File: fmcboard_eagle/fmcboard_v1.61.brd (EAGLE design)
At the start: 147 x 74 mm, 202 parts, among them IC1 OPA695IDR, IC10 LM358, IC11 7805TV, IC12 SN74AUC2G66DCTR, IC13 SN74AUC2G66DCTR, IC14 SN74AUC2G66DCTR, IC15 SN74AUC2G66DCTR, IC16 DAC7578SPWR, IC17 SN74AUC2G66DCTR, IC18 SN74AUC2G66DCTR, IC19 SN74AUC2G66DCTR, IC2 DAC7578SPWR, IC20 SN74AUC2G66DCTR, IC21 74AUP2GU04GW, IC22 74AUP2GU04GW, IC23 74AUP2GU04GW, IC24 74AUP2GU04GW, IC26 AMS1117-1.8, IC27 OPA699ID, IC3 LTC6229IMS8E#TRPBF, IC4 OPA695IDR, IC5 LTC6229IMS8E#TRPBF, IC6 OPA695IDR, IC7 OPA699ID, IC8 LM358, IC9 LM358, J1 8pin, J12 4p-2.54, J2 ASP-134604-01, J3 4p-2.54, J4 4p-2.54, J5 8pin, J6 4p-2.54, J7 4p-2.54, J8 4p-2.54, J9 8pin, U1 TXS0108EPWR, U2 STMICROELECTRONICS_L7905ACVST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

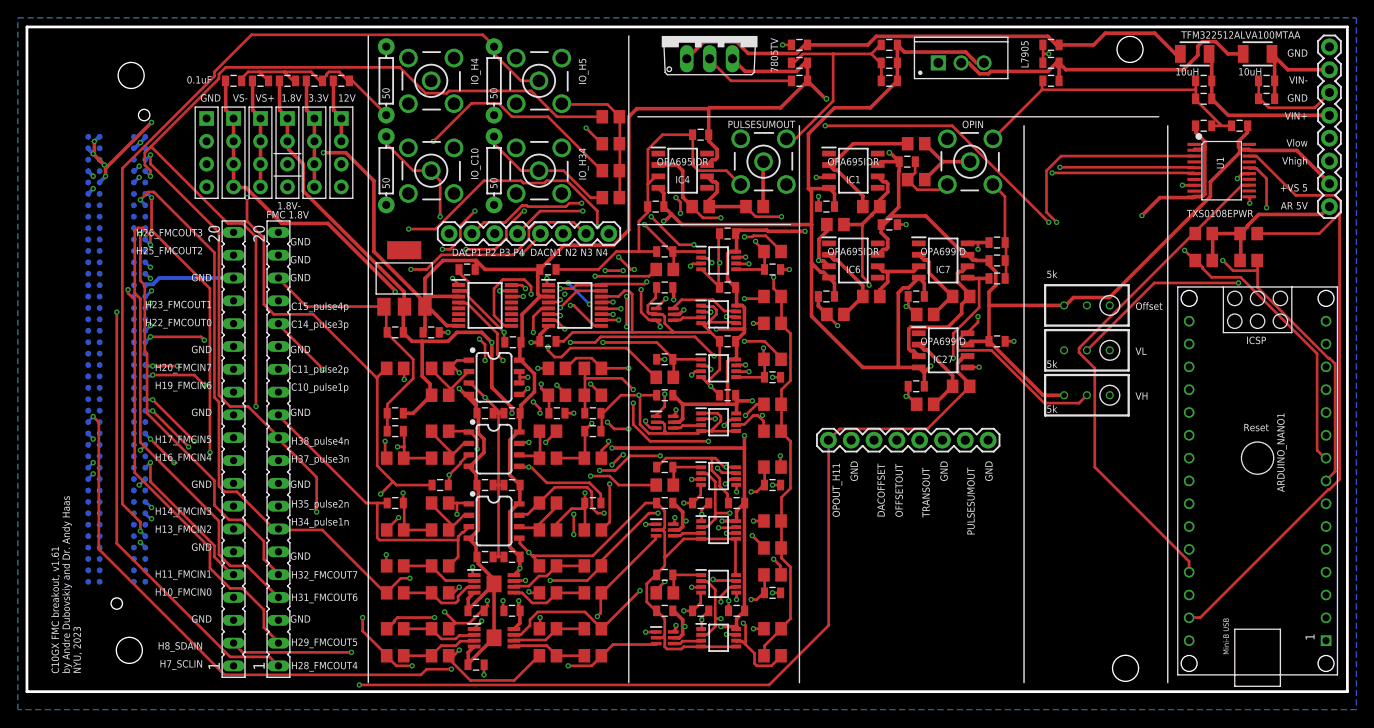
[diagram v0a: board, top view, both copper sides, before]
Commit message: use 1.8- and gnd for negative switches to gnd add 100 ohm resistors to inverting opa695s
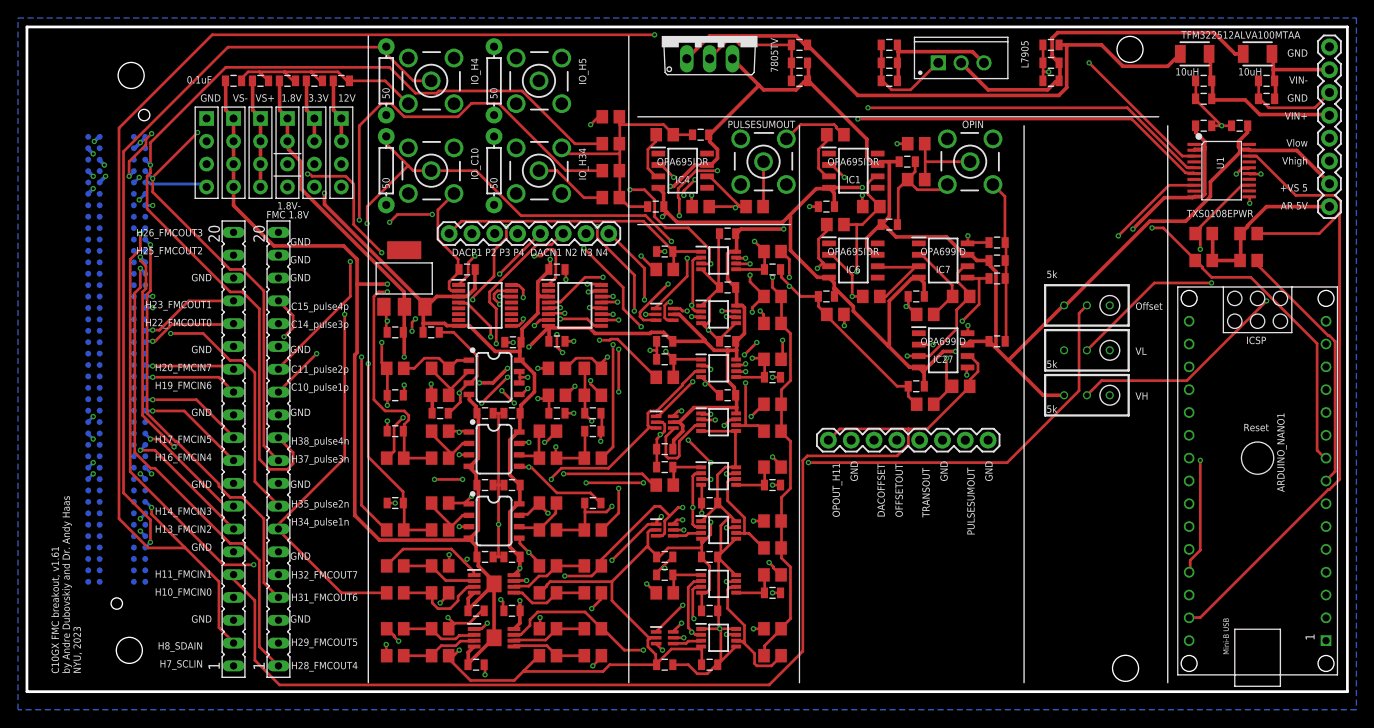
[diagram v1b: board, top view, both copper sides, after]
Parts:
- added R13, R3: 100, rcl:R0805
- moved C70 48.5 mm to (71.0, 3.00), turned to 0 degrees
- moved C35 42.6 mm to (78.0, 51.0)
- moved C77 31.0 mm to (76.0, 15.0)
- moved C36 26.9 mm to (46.0, 31.0), turned to 0 degrees
- moved C49 19.7 mm to (71.0, 27.0)
- moved C71 18.0 mm to (71.0, 15.0), turned to 0 degrees
- moved C51 12.0 mm to (76.0, 9.00)
- moved C34 9.00 mm to (41.0, 40.0)
- moved C66 7.00 mm to (41.0, 33.0), turned to 0 degrees
- moved C50 6.08 mm to (76.0, 3.00)
- moved C68 6.00 mm to (71.0, 39.0)
- moved C67 3.00 mm to (76.0, 21.0), turned to 0 degrees
- moved C14 1.00 mm to (59.0, 39.0)
- moved C54 1.00 mm to (59.0, 47.0)
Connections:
- removed net H10: J2.H10, SV1.4
- removed net OP2BUF: IC27.3, IC7.6, R6.2
- new net N$3: IC1.3, R3.1
- new net N$8: IC4.3, R13.1
- new net OPOUT_H10: IC27.3, IC7.6, J2.H10, R6.2, SV1.4
- net 1V8: no longer C66.1, C67.1, C70.1, C71.1, IC19.8, IC20.8, IC22.5, IC24.5
- net 1V8-: now also C66.1, C67.1, C70.1, C71.1, IC19.4, IC20.4, IC22.2, IC24.2
- net GND: now also IC19.8, IC20.8, IC22.5, IC24.5, R13.2, R3.2; no longer IC1.3, IC19.4, IC20.4, IC22.2, IC24.2, IC4.3
- net H34: no longer IC22.1
- net H34I: now also IC22.1
- net H35: no longer IC22.3
- net H35I: now also IC22.3
- net H37: no longer IC24.1
- net H37I: now also IC24.1
- net H38: no longer IC24.3
- net H38I: now also IC24.3
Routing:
- net OPOUT_H10: track 0.00 -> 147.1 mm, vias 0 -> 2
- net GND: track 524.9 -> 380.8 mm, vias 35 -> 42
- net C15: track 166.2 -> 92.0 mm, vias 4 -> 5
- net 1V8: track 260.9 -> 187.8 mm, vias 15 -> 7
- net SCLIN: track 209.8 -> 161.7 mm
- net H37: track 163.5 -> 120.3 mm, vias 5 -> 4
- net N$2: track 115.4 -> 74.3 mm, vias 7 -> 4
- net H34: track 154.4 -> 113.5 mm, vias 3 -> 2
- net SDAIN: track 174.6 -> 201.6 mm
- net VS+: track 301.5 -> 278.8 mm
- net VS-: track 259.7 -> 280.7 mm
- net C14: track 114.6 -> 94.3 mm, vias 8 -> 3
- net H10: track 17.8 -> 0.00 mm, vias 1 -> 0
- net AR_SDAIN2: track 150.7 -> 168.4 mm, vias 5 -> 4
- net OP2BUF: track 17.1 -> 0.00 mm
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
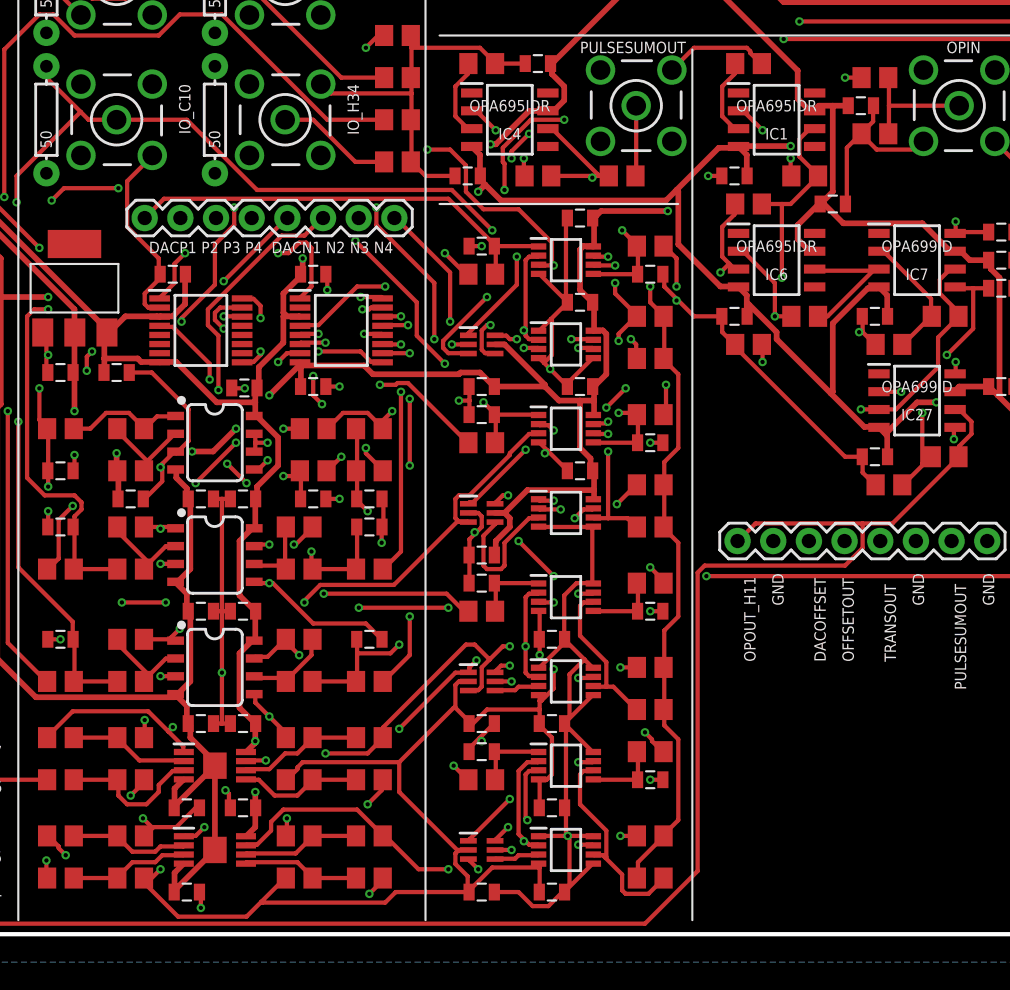
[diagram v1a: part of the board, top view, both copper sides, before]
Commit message: add dac pulse offsets + and -
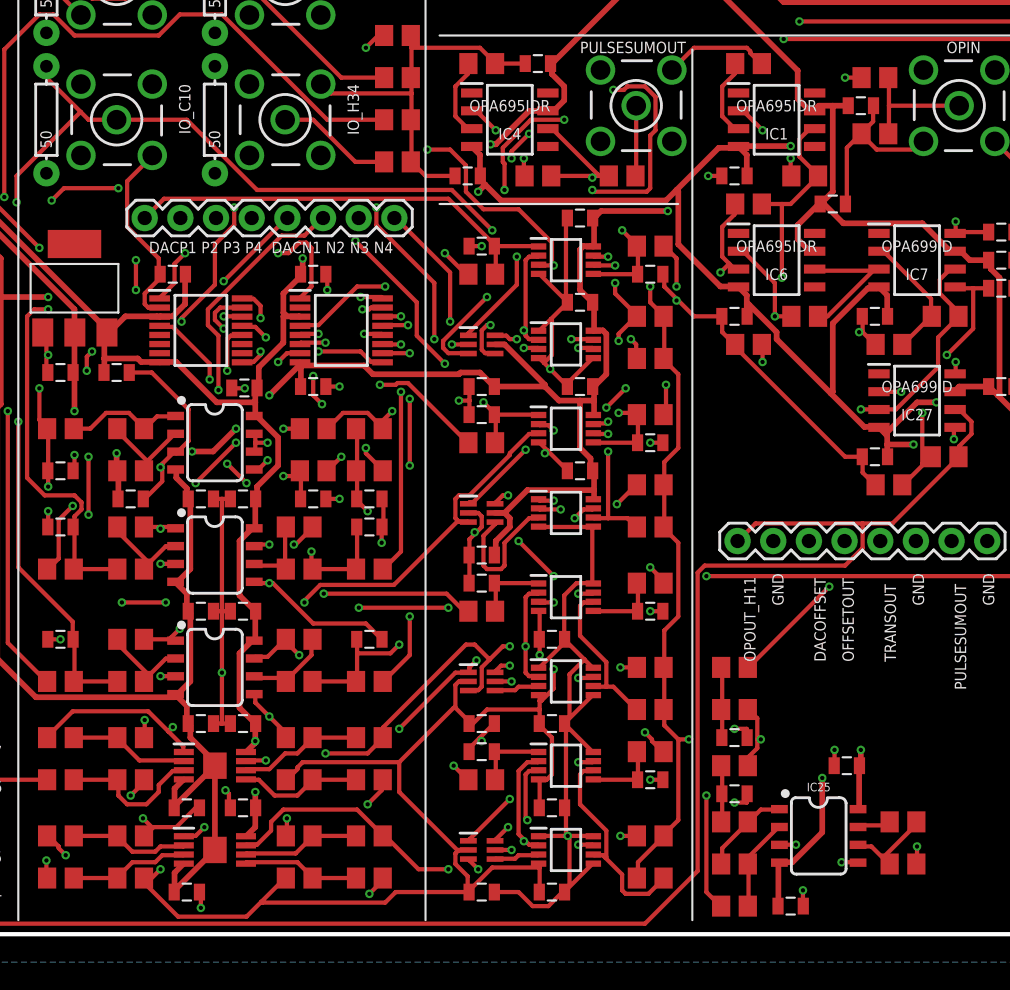
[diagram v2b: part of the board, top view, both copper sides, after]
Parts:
- added C11, C80: 1uF, SparkFun-Passives:0805
- added C33, C65: 0.1uF, SparkFun-Passives:0805
- added IC25: LM358, SparkFun-IC-Amplifiers:SO08
- added R14, R35, R61, R70, R79, R85: 1k, rcl:R0805
- added R73, R84: 100, rcl:R0805
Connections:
- new net N$30: IC25.7, R14.2
- new net N$36: IC25.1, R35.2, R73.2
- new net N$37: IC25.2, R35.1, R61.1
- new net N$38: IC25.6, R14.1, R70.1
- new net N$39: IC16.13, R84.2
- new net PULSEOFFSET_N: IC16.12, R61.2
- new net PULSEOFFSET_NI: C11.2, R73.1, R85.2
- new net PULSEOFFSET_P: C80.1, R79.2, R84.1
- net GND: now also C11.1, C33.2, C65.2, C80.2, IC25.3, IC25.5, R70.2
- net PULSESUMIN: now also R79.1, R85.1
- net VS+: now also C33.1, IC25.8
- net VS-: now also C65.1, IC25.4
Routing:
- net N$39: track 0.00 -> 121.9 mm, vias 0 -> 6
- net PULSEOFFSET_N: track 0.00 -> 94.0 mm, vias 0 -> 4
- net VS-: track 280.7 -> 325.2 mm, vias 4 -> 6
- net VS+: track 278.8 -> 310.3 mm, vias 5 -> 6
- net PULSESUMIN: track 65.5 -> 76.3 mm, vias 3 -> 5
- net GND: track 380.8 -> 389.8 mm, vias 42 -> 49
- net N$38: track 0.00 -> 6.99 mm
- net N$37: track 0.00 -> 6.69 mm
- net N$36: track 0.00 -> 6.44 mm
- net PULSEOFFSET_P: track 0.00 -> 5.20 mm
- net PULSEOFFSET_NI: track 0.00 -> 4.18 mm
- net N$30: track 0.00 -> 2.42 mm
